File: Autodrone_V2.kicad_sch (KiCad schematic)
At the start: 9 parts

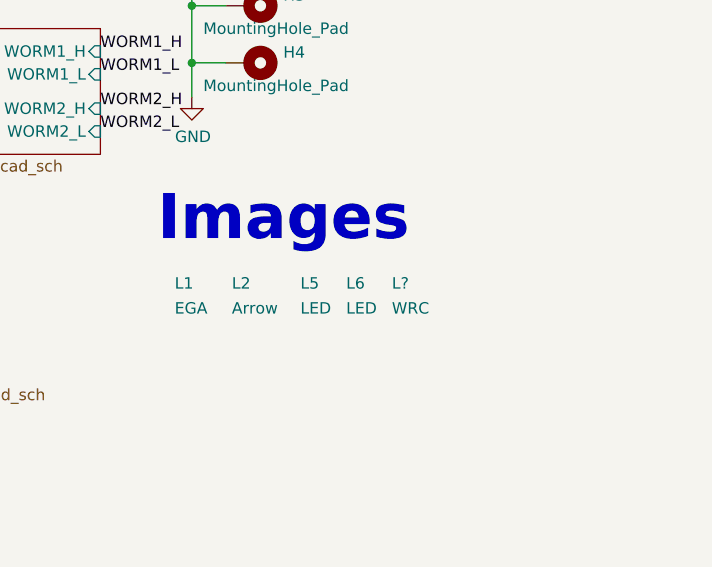
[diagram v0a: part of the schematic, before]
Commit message: Updated PDF of schematic
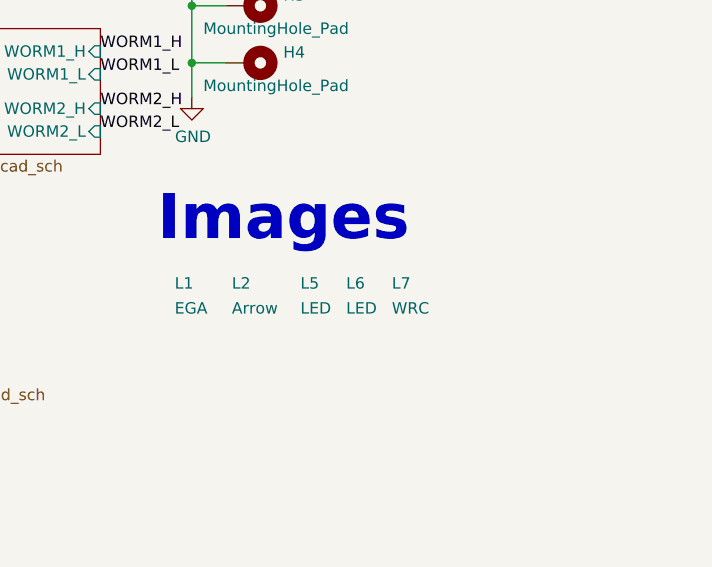
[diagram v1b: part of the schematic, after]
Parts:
- gave numbers to parts that had none: 1
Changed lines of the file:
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@@
   (symbol (lib_id "JPW_Symbols:WRC") (at 195.58 153.67 0) (unit 1)
     (in_bom yes) (on_board yes) (fields_autoplaced)
-    (property "Reference" "L?" (id 0) (at 196.215 152.7615 0)
+    (property "Reference" "L7" (id 0) (at 196.215 152.7615 0)
       (effects (font (size 1.27 1.27)) (justify left))
     )
@@
     )
     (path "/a25a0af3-ba5d-4626-b0bf-b638bab2a399"
-      (reference "L?") (unit 1) (value "WRC") (footprint "JPW_Footprints:WRC2")
+      (reference "L7") (unit 1) (value "WRC") (footprint "JPW_Footprints:WRC2")
     )
     (path "/00000000-0000-0000-0000-00006083bf4a/00000000-0000-0000-0000-00006086323c"

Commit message: I guess I made some changes
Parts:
- renumbered L5 to L3, L6 to L4, L7 to L5

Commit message: Added new files
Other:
- moved on the sheet: H1, H2, H3, H4
